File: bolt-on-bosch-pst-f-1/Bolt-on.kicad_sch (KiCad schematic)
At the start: 13 parts

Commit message: update board layout
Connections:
- net IO35: now also D1.2; no longer D1.1
- net IO36: now also D1.1; no longer D1.2
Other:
- moved on the sheet: D1
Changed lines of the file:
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@@
 	(symbol
 		(lib_id "Diode:BAT54C")
-		(at 270.51 205.74 180)
+		(at 270.51 205.74 0)
+		(mirror x)
 		(unit 1)
 		(exclude_from_sim no)
@@
 		)
 		(property "Footprint" "Package_TO_SOT_SMD:SOT-23_Handsoldering"
-			(at 268.605 208.915 0)
+			(at 272.415 208.915 0)
 			(effects
 				(font
@@
 		)
 		(property "Datasheet" "http://www.diodes.com/_files/datasheets/ds11005.pdf"
-			(at 272.542 205.74 0)
+			(at 268.478 205.74 0)
 			(effects
 				(font

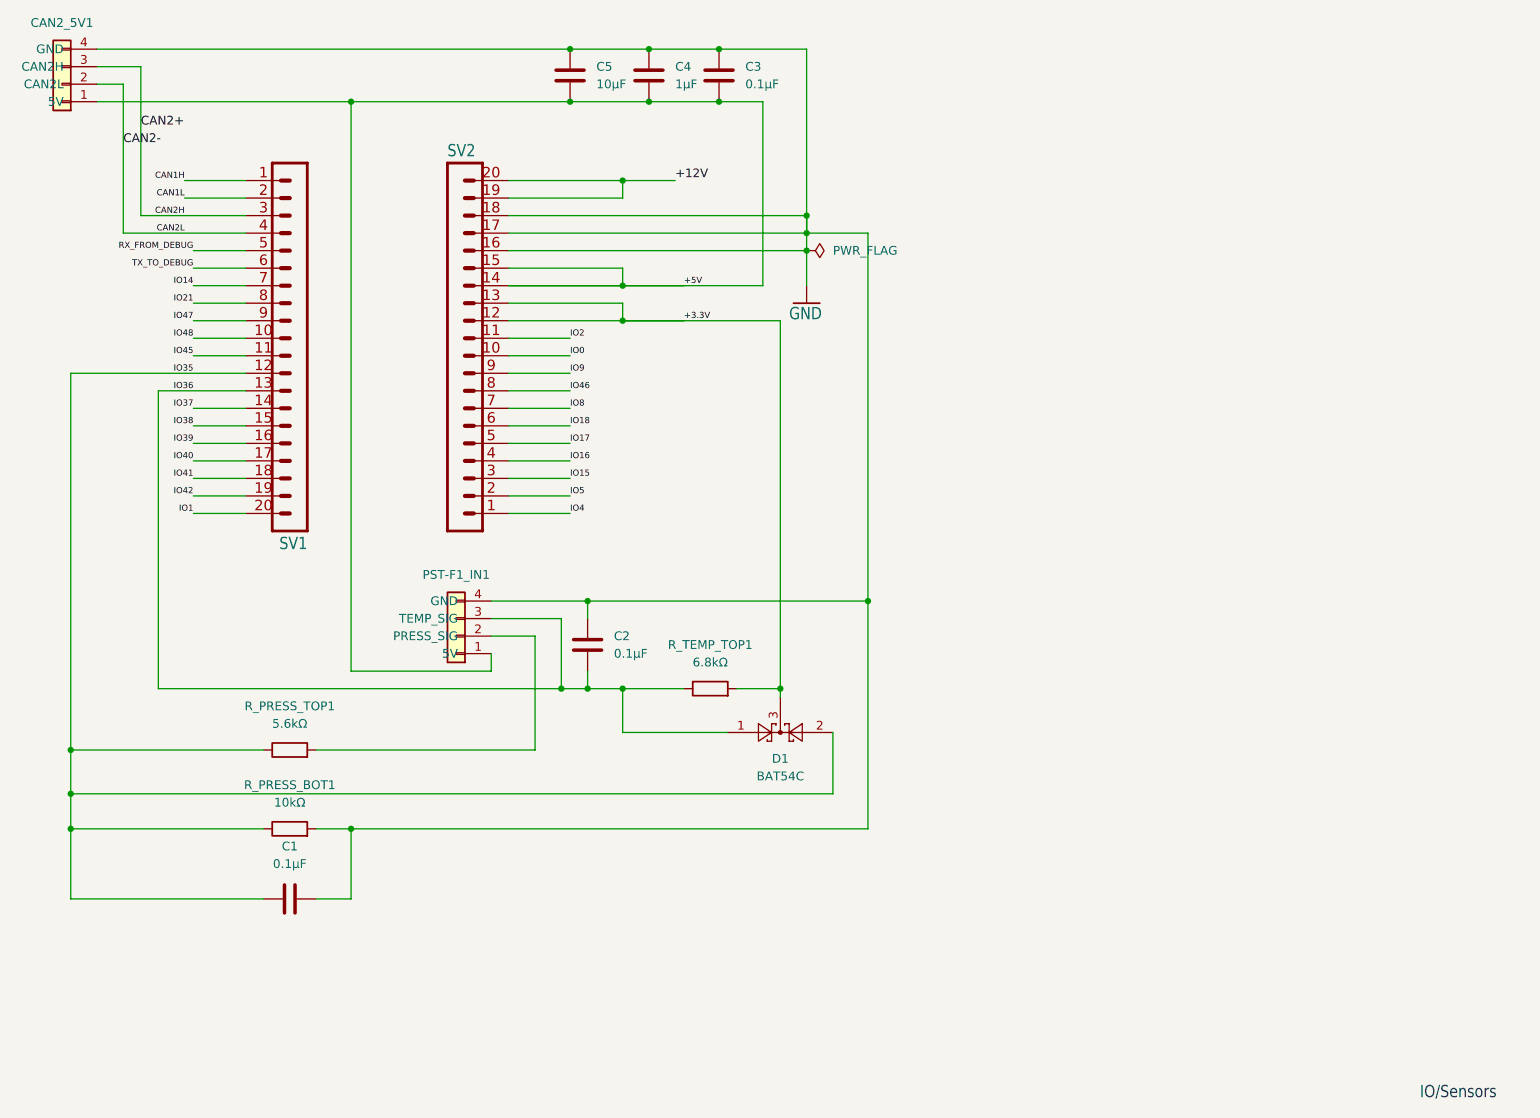
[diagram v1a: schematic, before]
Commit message: added low diode for proper clamp
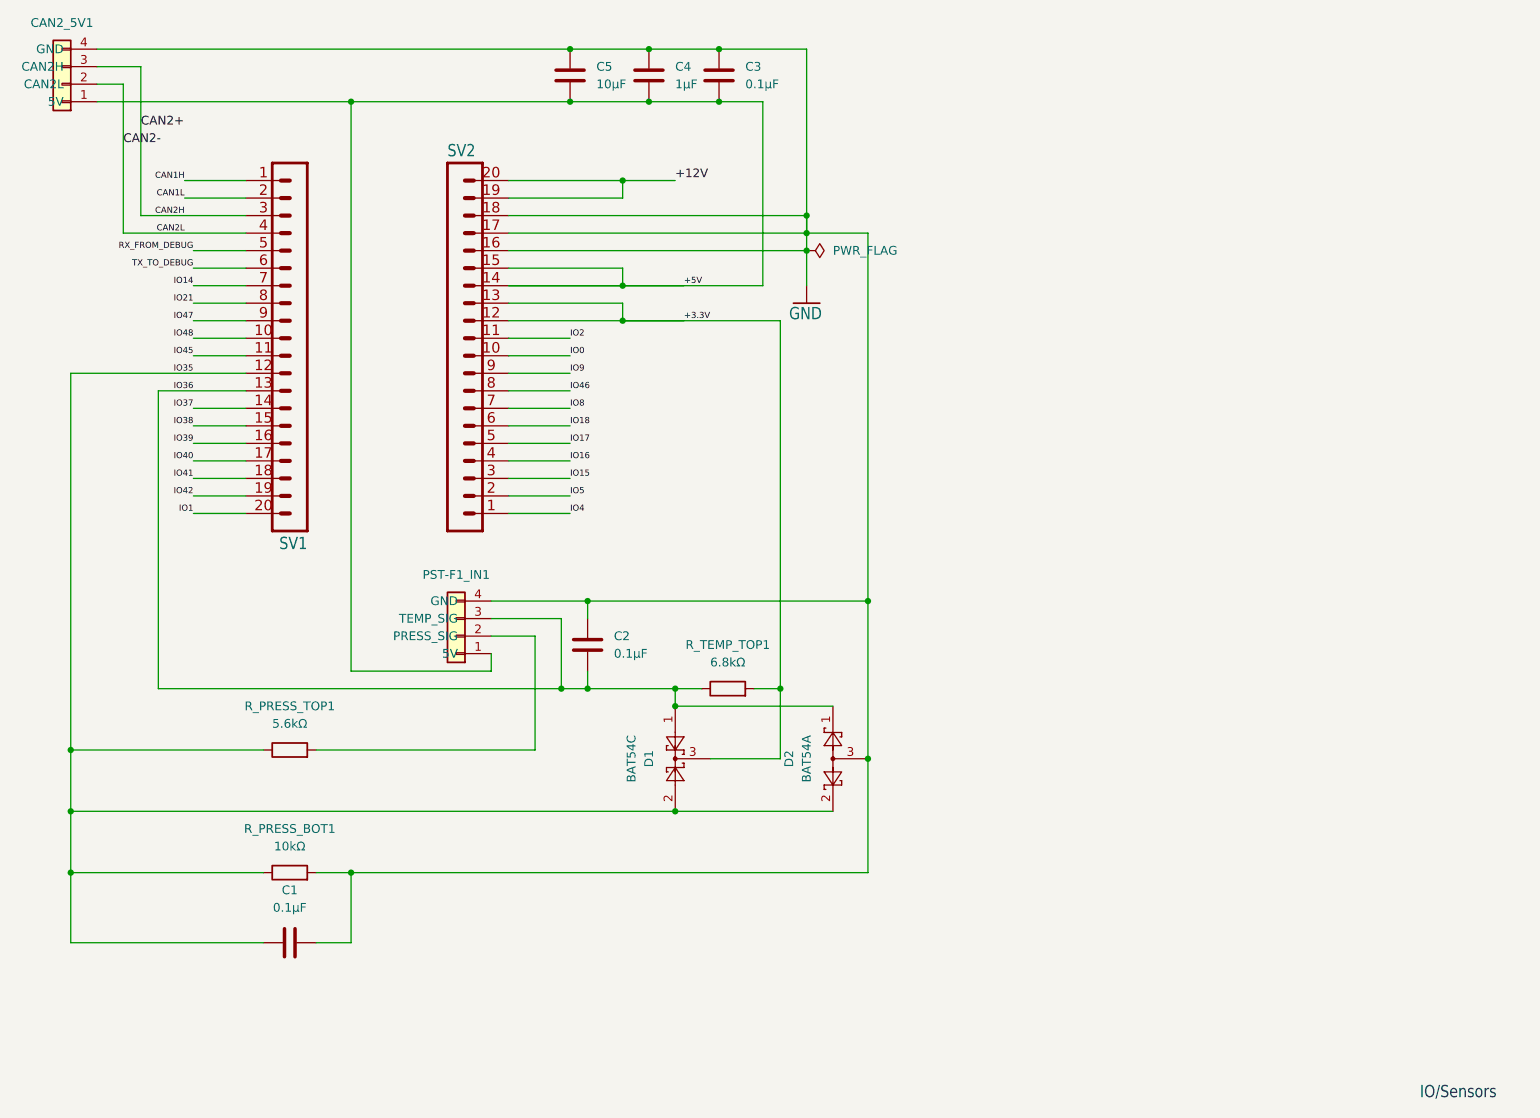
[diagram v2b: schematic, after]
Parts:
- added D2: BAT54A, Package_TO_SOT_SMD:TSOT-23_HandSoldering, symbol Diode:BAT54A
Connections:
- net GND: now also D2.3
- net IO35: now also D2.2
- net IO36: now also D2.1
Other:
- moved on the sheet: C1, D1, R_PRESS_BOT1, R_TEMP_TOP1

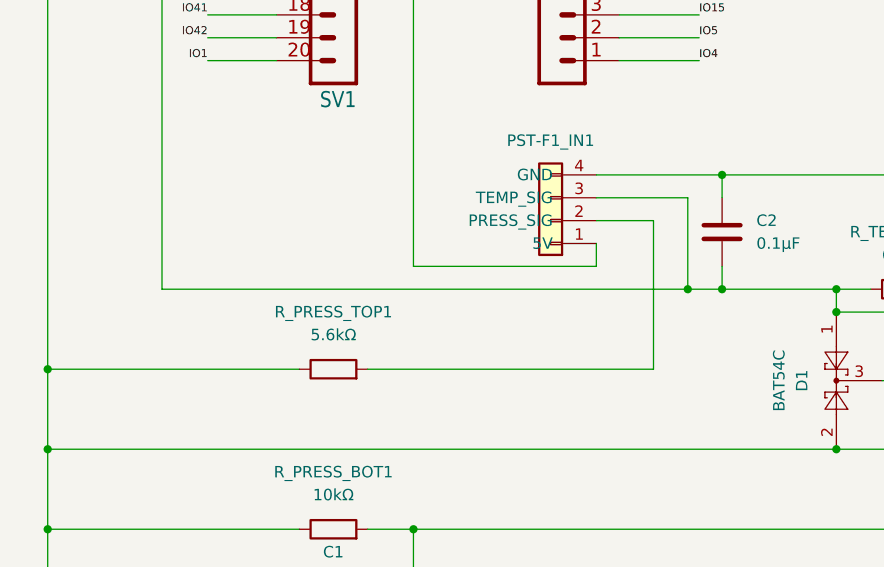
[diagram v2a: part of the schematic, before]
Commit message: pcb add ground copper pour on both sides
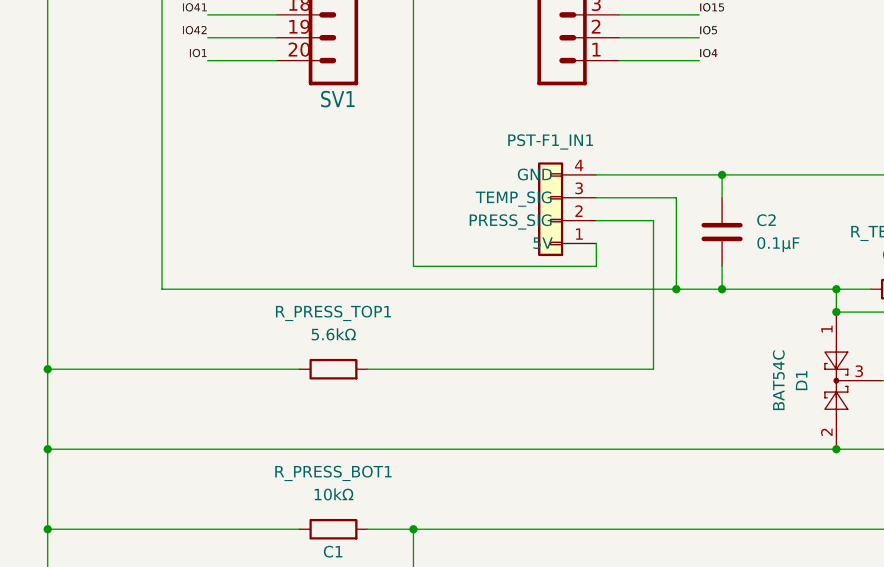
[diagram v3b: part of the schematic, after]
